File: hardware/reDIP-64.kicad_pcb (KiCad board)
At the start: 6 copper layers, 25.4 x 50.8 mm, 150 parts, among them J1 USB4080, J2 Conn_02x20_Counter_Clockwise, J3 Conn_01x20, J4 Conn_02x20_Odd_Even, J5 Conn_02x05_Odd_Even, Q1 PDTA143ZMB, SW1 KXT311LHS, U1 PTN5110NHQ, U10 FPF2495C, U11 TPS22916CN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

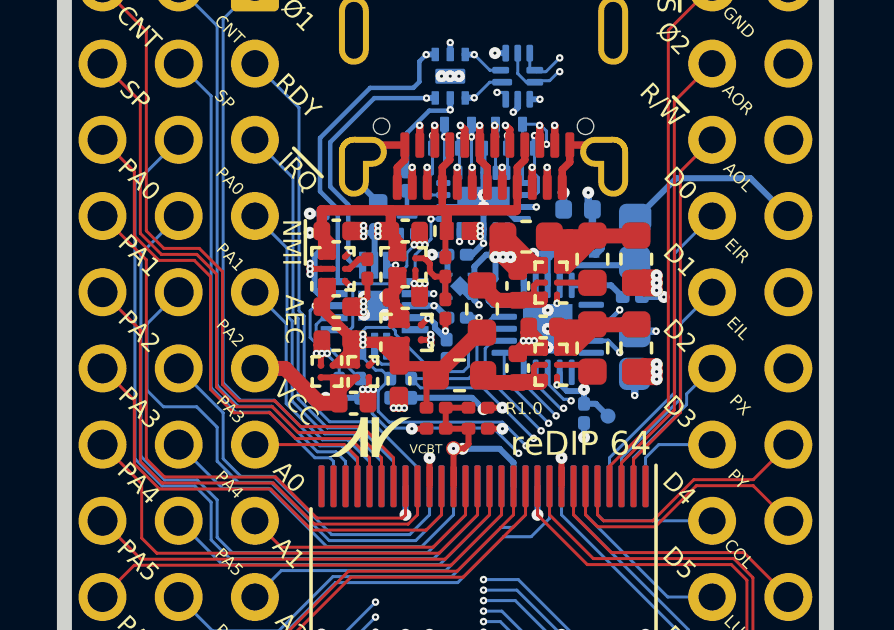
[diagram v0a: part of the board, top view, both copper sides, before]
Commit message: Further audio improvements
* Additional power supply vias
* Moved power and headphone out tracks away from under buck converters
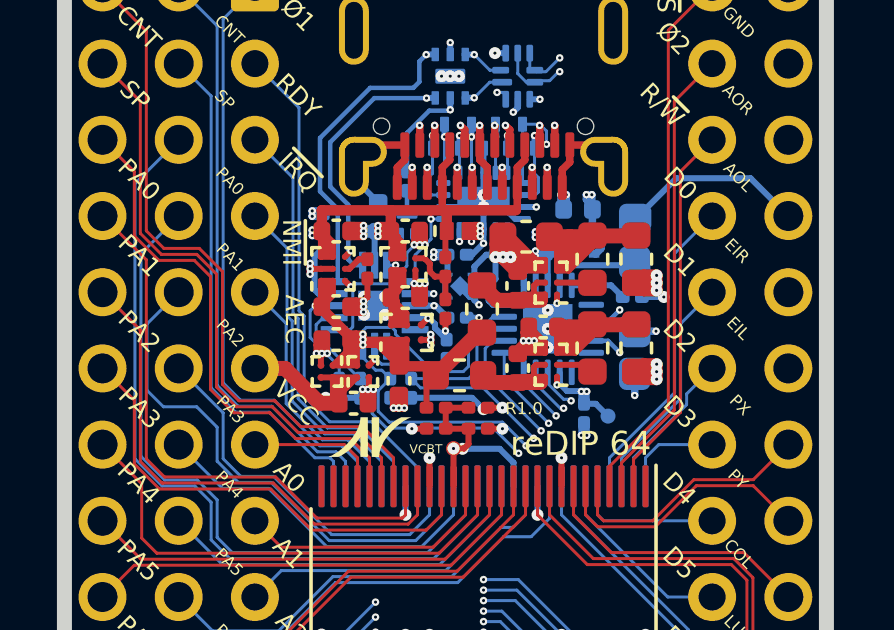
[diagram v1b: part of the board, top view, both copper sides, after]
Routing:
- net GND: track 166.1 -> 169.7 mm, vias 279 -> 285
- net +5V: track 51.8 -> 53.8 mm, vias 9 -> 11
- net VDDA: track 10.4 -> 12.0 mm, vias 4 -> 6
- net Net-(C69-Pad1): track 10.2 -> 8.85 mm
- net +3V3: track 80.8 -> 81.7 mm, vias 65 -> 66
- net VBUS: track 25.7 -> 26.6 mm, vias 5 -> 6
